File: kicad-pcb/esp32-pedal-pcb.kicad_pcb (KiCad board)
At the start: 4 copper layers, 216 x 25 mm, 49 parts, among them J1 USB_C_Receptacle_USB2.0_14P, J2 Conn_01x03, J3 Conn_01x03, Q1 Q_PMOS_GSD, SW1 SW_SPST, SW2 SW_SPDT, U1 MCP73871, U2 TLV75733PDBV, U3 ESP32-S3-WROOM-1, U4 TPD2EUSB30, U6 TPS2553DBVR

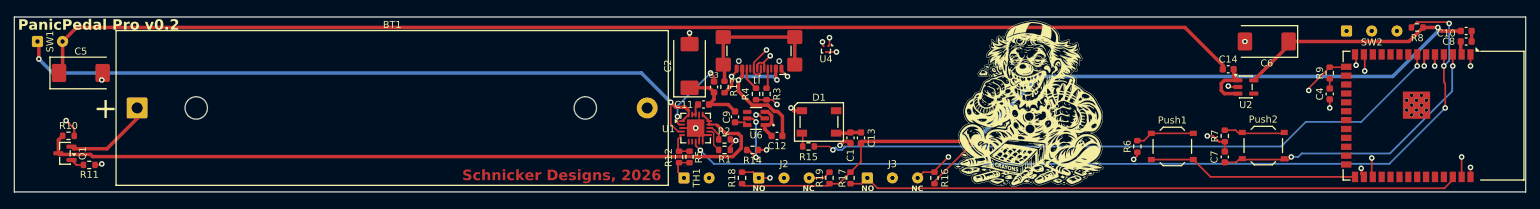
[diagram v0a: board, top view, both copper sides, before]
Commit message: Remove zip files and update PCB files
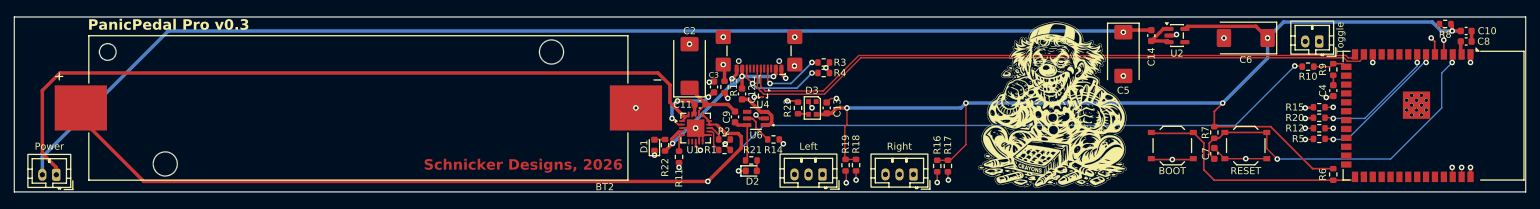
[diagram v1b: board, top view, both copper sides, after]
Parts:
- removed BT1: Battery_Cell, Battery:BatteryHolder_MPD_BH-18650-PC
- removed C1: 0.1µF, Capacitor_SMD:C_0603_1608Metric
- removed J2, J3: Conn_01x03, Connector_Wire:SolderWire-0.1sqmm_1x03_P3.6mm_D0.4mm_OD1mm
- removed Push1: BOOT, Button_Switch_SMD:SW_Push_1P1T_XKB_TS-1187A
- removed Push2: RESET, Button_Switch_SMD:SW_Push_1P1T_XKB_TS-1187A
- removed Q1: Q_PMOS_GSD, Package_TO_SOT_SMD:SOT-23
- removed TH1: NTC 10k, Connector_Wire:SolderWire-0.1sqmm_1x02_P3.6mm_D0.4mm_OD1mm
- added BOOT1: BOOT, Button_Switch_SMD:SW_Push_1P1T_XKB_TS-1187A, F.Cu at (199.0, 105.9)
- added BT2: 1042P, 1042P:BAT_1042P, F.Cu at (82.7, 100.5)
- added D2: LED, LED_SMD:LED_0603_1608Metric, F.Cu at (138.8, 109.5)
- added D3: WS2812B-2020, LED_SMD:LED_WS2812B-2020_PLCC4_2.0x2.0mm, F.Cu at (147.6, 100.5)
- added Pedal1: Conn_01x03, Connector_JST:JST_PH_B3B-PH-K_1x03_P2.00mm_Vertical, F.Cu at (149.0, 110.0)
- added Pedal2: Conn_01x03, Connector_JST:JST_PH_B3B-PH-K_1x03_P2.00mm_Vertical, F.Cu at (162.0, 110.0)
- added R20: 100Ω, Resistor_SMD:R_0603_1608Metric, F.Cu at (220.0, 101.9)
- added R21: 2.2kΩ, Resistor_SMD:R_0603_1608Metric, F.Cu at (138.8, 108.0)
- added R22: 2.2kΩ, Resistor_SMD:R_0603_1608Metric, F.Cu at (126.5, 105.8)
- added R23: 220Ω, Resistor_SMD:R_0603_1608Metric, F.Cu at (145.5, 100.5)
- added RESET1: RESET, Button_Switch_SMD:SW_Push_1P1T_XKB_TS-1187A, F.Cu at (209.5, 105.9)
- D1: value Inolux_IN-PI554FCH -> LED; footprint LED_SMD:LED_Inolux_IN-PI554FCH_PLCC4_5.0x5.0mm_P3.2mm -> LED_SMD:LED_0603_1608Metric
- R1: value 3.32kΩ -> 2.0kΩ
- R10: value 100kΩ -> 360kΩ
- R11: value 100kΩ -> 10kΩ
- R12: value 69.8kΩ -> 100Ω
- R14: value 100kΩ -> 49.9k
- R15: value 300Ω -> 100Ω
- R2: value 33kΩ -> 20kΩ
- R5: value 1.54kΩ -> 100Ω
- R9: value 360kΩ -> 100kΩ
- SW1: footprint Connector_Wire:SolderWire-0.1sqmm_1x02_P3.6mm_D0.4mm_OD1mm -> Connector_JST:JST_PH_B2B-PH-K_1x02_P2.00mm_Vertical
- SW2: value SW_SPDT -> SW_SPST; footprint Connector_Wire:SolderWire-0.1sqmm_1x03_P3.6mm_D0.4mm_OD1mm -> Connector_JST:JST_PH_B2B-PH-K_1x02_P2.00mm_Vertical
- moved R10 177.4 mm to (218.4, 94.6)
- moved C5 149.0 mm to (192.0, 92.8), turned to -90 degrees
- moved R12 91.6 mm to (220.0, 103.4), turned to 0 degrees
- moved R5 90.0 mm to (220.0, 104.9), turned to 180 degrees
- moved R11 84.3 mm to (128.5, 107.5), turned to -90 degrees
- moved R15 73.2 mm to (220.0, 100.4), turned to 0 degrees
- moved R6 28.3 mm to (222.0, 110.0), turned to -90 degrees
- moved D1 23.7 mm to (125.0, 105.8), turned to 90 degrees
- moved SW1 19.2 mm to (39.5, 110.0), turned to 180 degrees
- moved R18 16.4 mm to (153.8, 108.7), turned to -90 degrees
- moved R17 14.0 mm to (166.9, 108.8)
- moved U2 12.3 mm to (199.7, 90.2)
- moved C14 12.0 mm to (196.0, 90.2), turned to -90 degrees
- moved U4 11.1 mm to (140.5, 98.5)
- moved R4 10.1 mm to (149.2, 95.5), turned to 180 degrees
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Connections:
- net /DATA+ renamed /D+
- net /DATA- renamed /D-
- net /MCP OUT 5V SWITCHED renamed /5V SWITCHED
- net Net-(U1-STAT1/~{LBO}) renamed /GPIO4/LBO
- net Net-(U3-GPIO3/TOUCH3/ADC1_CH2) renamed /GPIO3
- net Net-(U6-OUT) renamed /TPS OUT
- C11 pad 1: Net-(C11-Pad1) -> Net-(U1-CE)
- C11 pad 2: Net-(C11-Pad2) -> /MCP IN
- C13 pad 2: Net-(D1-VDD) -> GND
- C2 pad 1: Net-(C11-Pad1) -> Net-(U1-CE)
- C3 pad 1: Net-(C11-Pad1) -> /MCP IN
- C3 pad 2: Net-(U1-VPCC) -> GND
- C7 pad 1: GND -> /EN
- C7 pad 2: /RESET -> GND
- C9 pad 2: Net-(C11-Pad1) -> Net-(U1-CE)
- D1 pad 2: Net-(D1-DIN) -> Net-(D1-A)
- R11 pad 1: /GATE -> /THERM
- R12 pad 1: Net-(U1-THERM) -> Net-(Pedal1-Pin_1)
- R12 pad 2: Net-(R12-Pad2) -> /GPIO2
- R15 pad 1: /Led DIN -> Net-(Pedal2-Pin_1)
- R15 pad 2: Net-(D1-DIN) -> /GPIO1
- R16 pad 1: /3V3 -> Net-(Pedal2-Pin_3)
- R16 pad 2: Net-(J3-Pin_3) -> /3V3
- R17 pad 2: Net-(J3-Pin_1) -> Net-(Pedal2-Pin_1)
- R18 pad 2: Net-(J2-Pin_1) -> Net-(Pedal1-Pin_1)
- R19 pad 1: /3V3 -> Net-(Pedal1-Pin_3)
- R19 pad 2: Net-(J2-Pin_3) -> /3V3
- R5 pad 1: Net-(U1-THERM) -> /GPIO6
- R5 pad 2: Net-(R12-Pad2) -> Net-(Pedal1-Pin_3)
- R6 pad 1: GND -> /3V3
- R6 pad 2: Net-(Push1-Pad1) -> /GPIO0
- R7 pad 1: GND -> /3V3
- R7 pad 2: Net-(Push2-Pad1) -> /EN
- SW1 pad 1: /MCP OUT 5V -> /5V
- SW2 pad 1: Net-(SW2-A) -> /GPIO5
- U1 pad 1: /MCP OUT 5V -> /5V
- U1 pad 17: GND -> Net-(U1-CE)
- U1 pad 18: Net-(C11-Pad2) -> /MCP IN
- U1 pad 19: Net-(C11-Pad2) -> /MCP IN
- U1 pad 2: Net-(U1-VPCC) -> /MCP IN
- U1 pad 20: /MCP OUT 5V -> /5V
- U1 pad 4: /MCP OUT 5V -> /VBUS
- U1 pad 5: Net-(U1-THERM) -> /THERM
- U3 pad 12: unconnected-(U3-GPIO8/TOUCH8/ADC1_CH7/SUBSPICS1-Pad12) -> /GPIO8
- U3 pad 27: /BOOT -> /GPIO0
- U3 pad 28: Net-(J2-Pin_3) -> unconnected-(U3-SPIIO6/GPIO35/FSPID/SUBSPID-Pad28)
- U3 pad 29: Net-(J3-Pin_3) -> unconnected-(U3-SPIIO7/GPIO36/FSPICLK/SUBSPICLK-Pad29)
- U3 pad 3: /RESET -> /EN
- U3 pad 38: Net-(J3-Pin_1) -> /GPIO2
- U3 pad 39: Net-(J2-Pin_1) -> /GPIO1
- U3 pad 5: Net-(SW2-C) -> /GPIO5
- U3 pad 6: Net-(SW2-A) -> /GPIO6
- U3 pad 7: /Led DIN -> /GPIO7
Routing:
- net /GPIO3: track 190.4 -> 5.08 mm, vias 2 -> 0
- net /5V: track 0.00 -> 111.1 mm
- net Net-(J2-Pin_1): track 107.3 -> 0.00 mm, vias 2 -> 0
- net /MCP OUT 5V: track 105.6 -> 0.00 mm, vias 2 -> 0
- net /GPIO8: track 0.00 -> 96.4 mm, vias 0 -> 2
- net /VBAT: track 109.8 -> 205.5 mm, vias 0 -> 2
- net /Led DIN: track 93.4 -> 0.00 mm, vias 2 -> 0
- net Net-(J3-Pin_1): track 88.0 -> 0.00 mm
- net Net-(J2-Pin_3): track 86.0 -> 0.00 mm, vias 1 -> 0
- net Net-(Pedal1-Pin_3): track 0.00 -> 80.3 mm, vias 0 -> 2
- net Net-(J3-Pin_3): track 79.6 -> 0.00 mm, vias 2 -> 0
- net Net-(Pedal1-Pin_1): track 0.00 -> 76.0 mm, vias 0 -> 2
- net Net-(Pedal2-Pin_3): track 0.00 -> 68.6 mm, vias 0 -> 2
- net Net-(Pedal2-Pin_1): track 0.00 -> 64.5 mm, vias 0 -> 2
- net /EN: track 0.00 -> 50.7 mm, vias 0 -> 2
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- added copper zone on In1.Cu, net GND
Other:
- board text added: "PanicPedal Pro v0.3"
- board text removed: "C7"
- board text removed: "NC"
- board text removed: "NO"
- board text removed: "PanicPedal Pro v0.2"

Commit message: Standardize debug message formatting and add debug monitor support
- Created shared debug_format.h/cpp for consistent debug message formatting
- Updated transmitter and receiver to use shared debug formatting code
- Debug messages now use format: [MAC] [R/T] [timestamp] message
- MAC address shown by debug monitor from ESP-NOW packet info
- Added NVRAM persistence for debug toggle state on FireBeetle 2
- Transmitter sends debug messages to debug monitor when debug enabled
- Fixed debug monitor persistence loading/saving in receiver
- Updated all pedal event messages to use standardized format
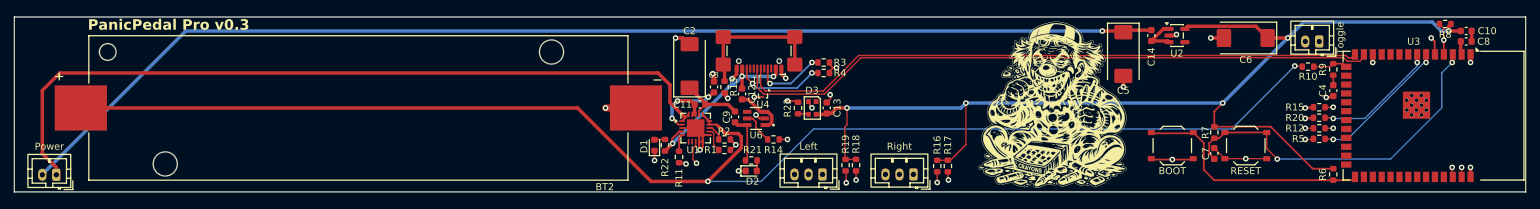
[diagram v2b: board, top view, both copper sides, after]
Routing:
- net GND: track 53.3 -> 67.6 mm
- net /GPIO4/LBO: track 120.3 -> 123.6 mm
- net /5V SWITCHED: track 168.7 -> 167.0 mm
- net /3V3: track 156.6 -> 157.8 mm
- net /VBAT: track 205.5 -> 204.6 mm
- net /SHIELD: track 21.9 -> 21.5 mm, vias 4 -> 0
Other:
- board text removed: "Schnicker Designs, 2026"

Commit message: Fix watchdog timeouts and stabilize interrupt handling
- Simplified interrupt handling: removed interrupt detachment/reattachment
- Reduced debounce time from 200ms to 50ms for better responsiveness
- Removed excessive yield() calls that were causing instability
- Fixed panic issues when pedal is held down
- Fixed panic issues when pedal is not paired
- Fixed activity timer reset when pedal is pressed
- Improved ESP-NOW send reliability with proper peer management
- Cleaned up code and removed debug heartbeat messages
- Restored 5-minute inactivity timeout for deep sleep
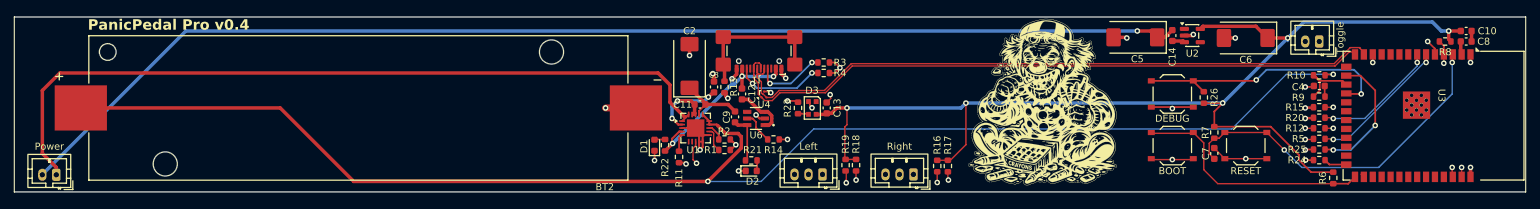
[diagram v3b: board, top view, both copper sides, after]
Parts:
- added DEBUG1: TS-1187A-C-E-B, Button_Switch_SMD:SW_Push_1P1T_XKB_TS-1187A, F.Cu at (199.0, 98.5)
- added R24: 100kΩ, Resistor_SMD:R_0603_1608Metric, F.Cu at (220.0, 108.0)
- added R25: 100kΩ, Resistor_SMD:R_0603_1608Metric, F.Cu at (220.0, 106.4)
- added R26: 10kΩ, Resistor_SMD:R_0603_1608Metric, F.Cu at (203.5, 99.0)
- BOOT1: value BOOT -> TS-1187A-C-E-B
- BT2: value 1042P -> Keystone 1042P
- D1: value LED -> 19-217/R6C-AL1M2VY/3T
- D2: value LED -> 19-217/GHC-YR1S2/3T
- Pedal1, Pedal2: value Conn_01x03 -> B3B-PH-K-S(LF)(SN)
- RESET1: value RESET -> TS-1187A-C-E-B
- SW1, SW2: value SW_SPST -> B2B-PH-K-S(LF)(SN)
- U1: value MCP73871 -> MCP73871T-2CCI/ML
- U3: value ESP32-S3-WROOM-1 -> ESP32-S3-WROOM-1-N8
- U4: value TPD2EUSB30 -> TPD2EUSB30ADRTR
- moved R9 4.36 mm to (220.0, 98.9), turned to 180 degrees
- moved C14 3.00 mm to (199.0, 90.2)
- moved C5 2.95 mm to (193.7, 90.4), turned to 180 degrees
- moved R8 2.50 mm to (238.0, 91.0)
- moved U2 2.20 mm to (201.9, 90.2)
- moved C4 2.11 mm to (220.0, 97.4), turned to 0 degrees
- moved R10 2.03 mm to (220.0, 95.8), turned to 180 degrees
- moved R6 0.50 mm to (222.0, 110.5)
- moved U4 0.17 mm to (140.7, 98.6), turned to 0 degrees
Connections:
- R10 pad 2: /GPIO3 -> /GPIO9
- R9 pad 2: /GPIO3 -> /GPIO9
- U3 pad 15: /GPIO3 -> unconnected-(U3-GPIO3/TOUCH3/ADC1_CH2-Pad15)
- U3 pad 16: unconnected-(U3-GPIO46-Pad16) -> /GPIO46
- U3 pad 17: unconnected-(U3-GPIO9/TOUCH9/ADC1_CH8/FSPIHD/SUBSPIHD-Pad17) -> /GPIO9
- U3 pad 18: unconnected-(U3-GPIO10/TOUCH10/ADC1_CH9/FSPICS0/FSPIIO4/SUBSPICS0-Pad18) -> /GPIO10
- U3 pad 26: unconnected-(U3-GPIO45-Pad26) -> /GPIO45
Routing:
- net /GPIO10: track 0.00 -> 38.2 mm, vias 0 -> 2
- net /GPIO46: track 0.00 -> 18.7 mm, vias 0 -> 2
- net /GPIO9: track 0.00 -> 10.2 mm
- net GND: track 67.6 -> 77.4 mm, vias 25 -> 28
- net /GPIO3: track 5.08 -> 0.00 mm
- net /VBAT: track 204.6 -> 209.7 mm
- net /D+: track 90.2 -> 95.0 mm
- net Net-(U2-EN): track 5.84 -> 1.80 mm
- net /GPIO4/LBO: track 123.6 -> 119.6 mm
- net /5V SWITCHED: track 167.0 -> 170.8 mm
- net /GPIO45: track 0.00 -> 3.63 mm
- net /D-: track 92.8 -> 96.4 mm
- net /3V3: track 157.8 -> 159.9 mm
- net /GPIO5: track 18.8 -> 17.8 mm
- net /EN: track 50.7 -> 50.0 mm
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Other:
- board text added: "PanicPedal Pro v0.4"
- board text removed: "PanicPedal Pro v0.3"
